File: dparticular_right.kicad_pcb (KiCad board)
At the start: 2 copper layers, 185.7 x 157.2 mm, 51 parts, among them J1 To Left Hand, SW1:10 Key_Ins, SW1:11 Key_Prnt, SW2:10 Key_F7, SW2:11 Key_F8, SW2:12 Key_F9, SW2:13 Key_F10, SW2:14 Key_F11, SW2:15 Key_F12, SW2:16 Key_Del, SW3:10 Key_7, SW3:11 Key_8, SW3:12 Key_9, SW3:13 Key_0, SW3:14 Key_Hyph, SW3:15 Key_Eql, SW3:16 Key_Bksp, SW3:9 Key_6, SW4:10 Key_U, SW4:11 Key_I, SW4:12 Key_O, SW4:13 Key_P, SW4:14 Key_LBrk, SW4:15 Key_RBrk, SW4:16 Key_BkSl, SW4:9 Key_Y, SW5:10 Key_J, SW5:11 Key_K, SW5:12 Key_L, SW5:13 Key_Semi, SW5:14 Key_Quot, SW5:16 Key_Entr, SW5:9 Key_H, SW6:10 Key_M, SW6:11 Key_Coma, SW6:12 Key_Per, SW6:13 Key_Slsh, SW6:14 Key_RShft, SW6:9 Key_N, SW7:11 Key_RAlt, SW7:12 Key_RWin, SW7:13 Key_Menu, SW7:14 Key_RCtrl, SW7:9 Key_RSpc, U1 MCP23018

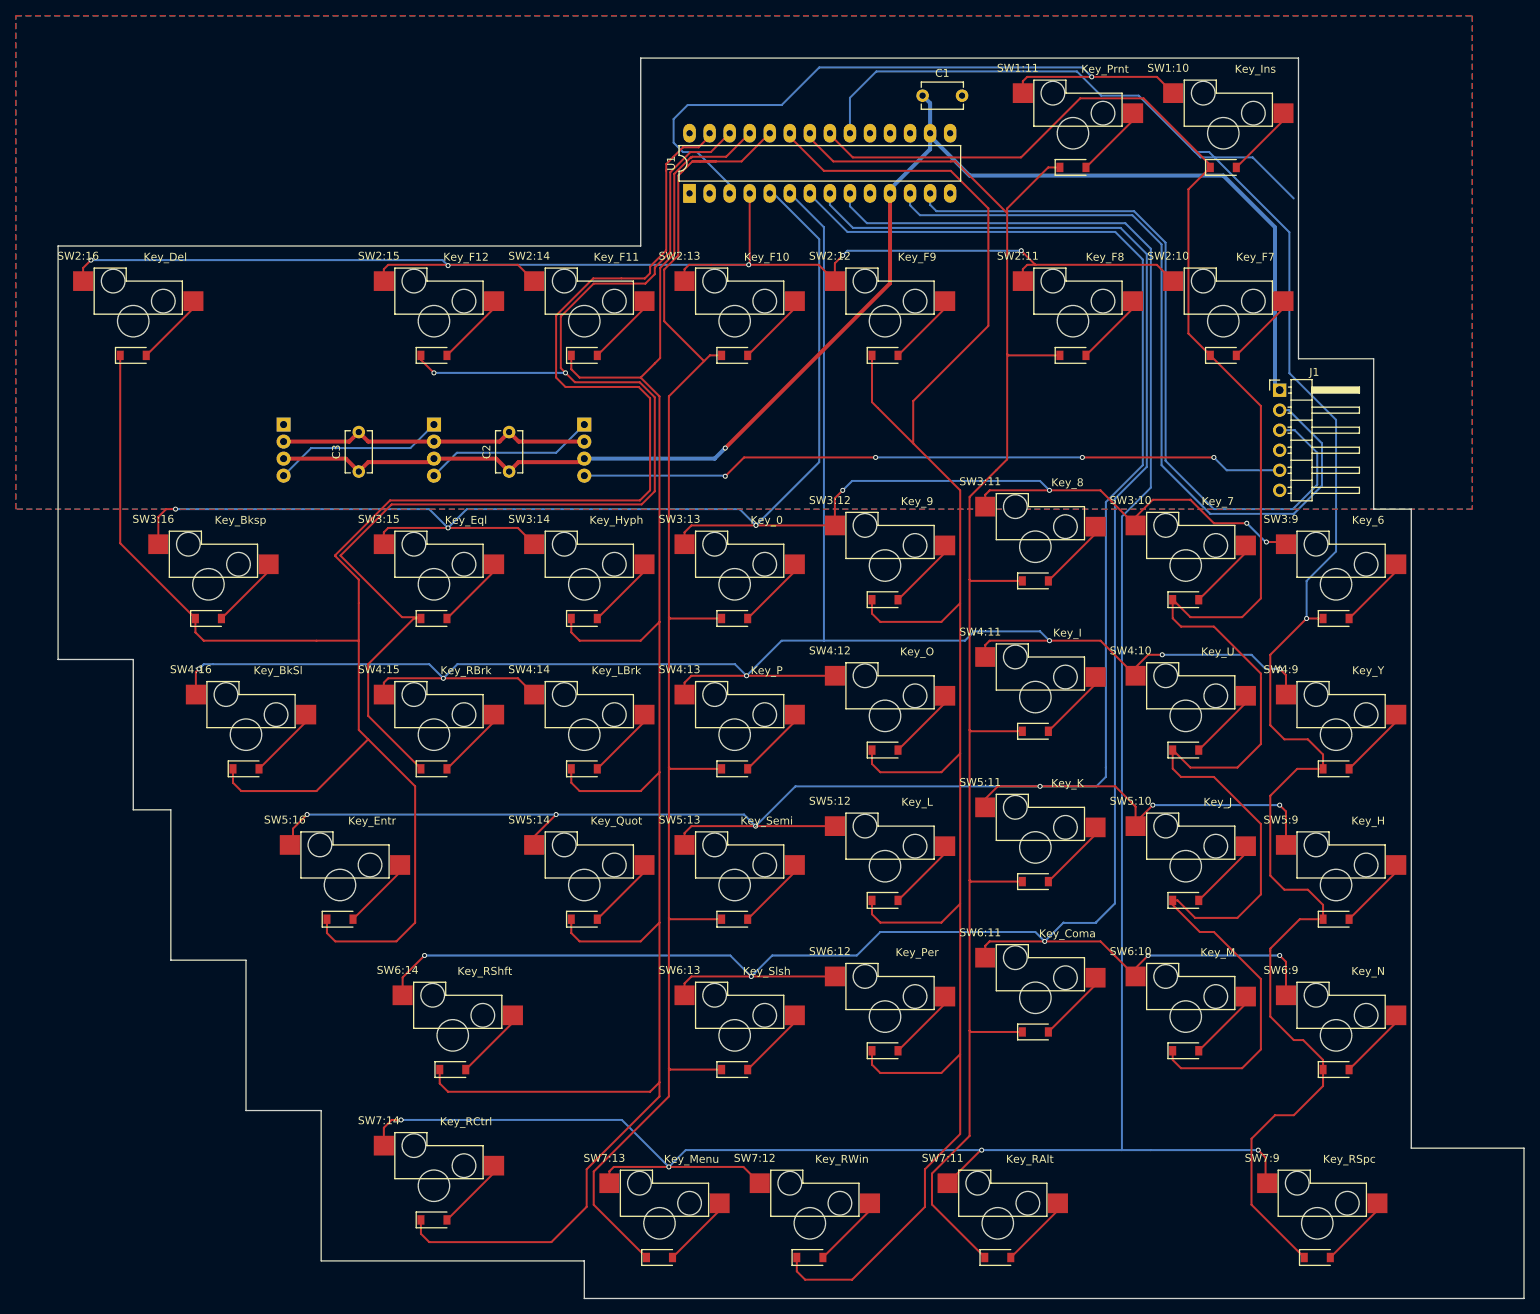
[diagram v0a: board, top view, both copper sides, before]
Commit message: Right hand: eliminate right angles in remaining columns
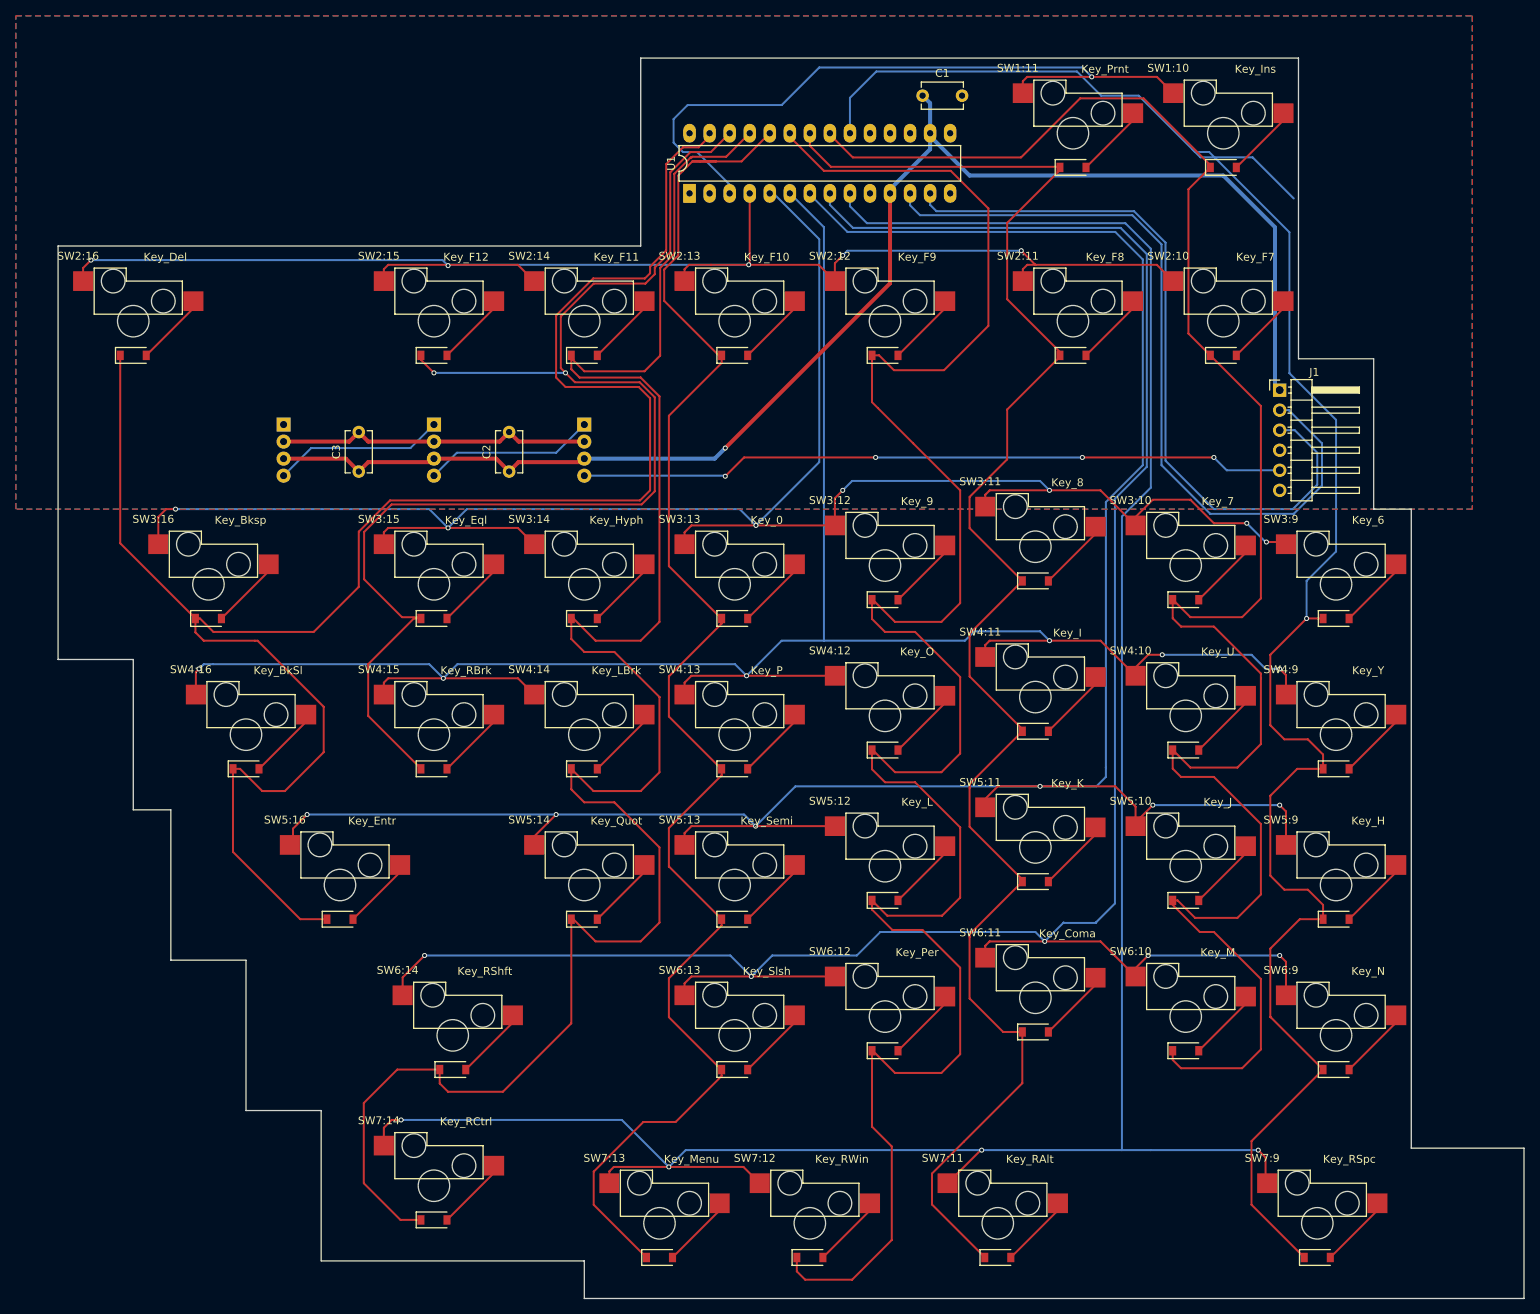
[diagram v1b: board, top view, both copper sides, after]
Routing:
- net /COL16: track 259.3 -> 244.1 mm
- net /COL12: track 257.1 -> 270.6 mm
- net /COL14: track 258.8 -> 250.5 mm
- net /COL13: track 194.8 -> 192.0 mm
- net /COL15: track 170.7 -> 168.2 mm
- net /COL9: track 253.7 -> 251.7 mm
- net /COL11: track 211.8 -> 211.1 mm

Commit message: Right hand: Eliminate all remaining right angles
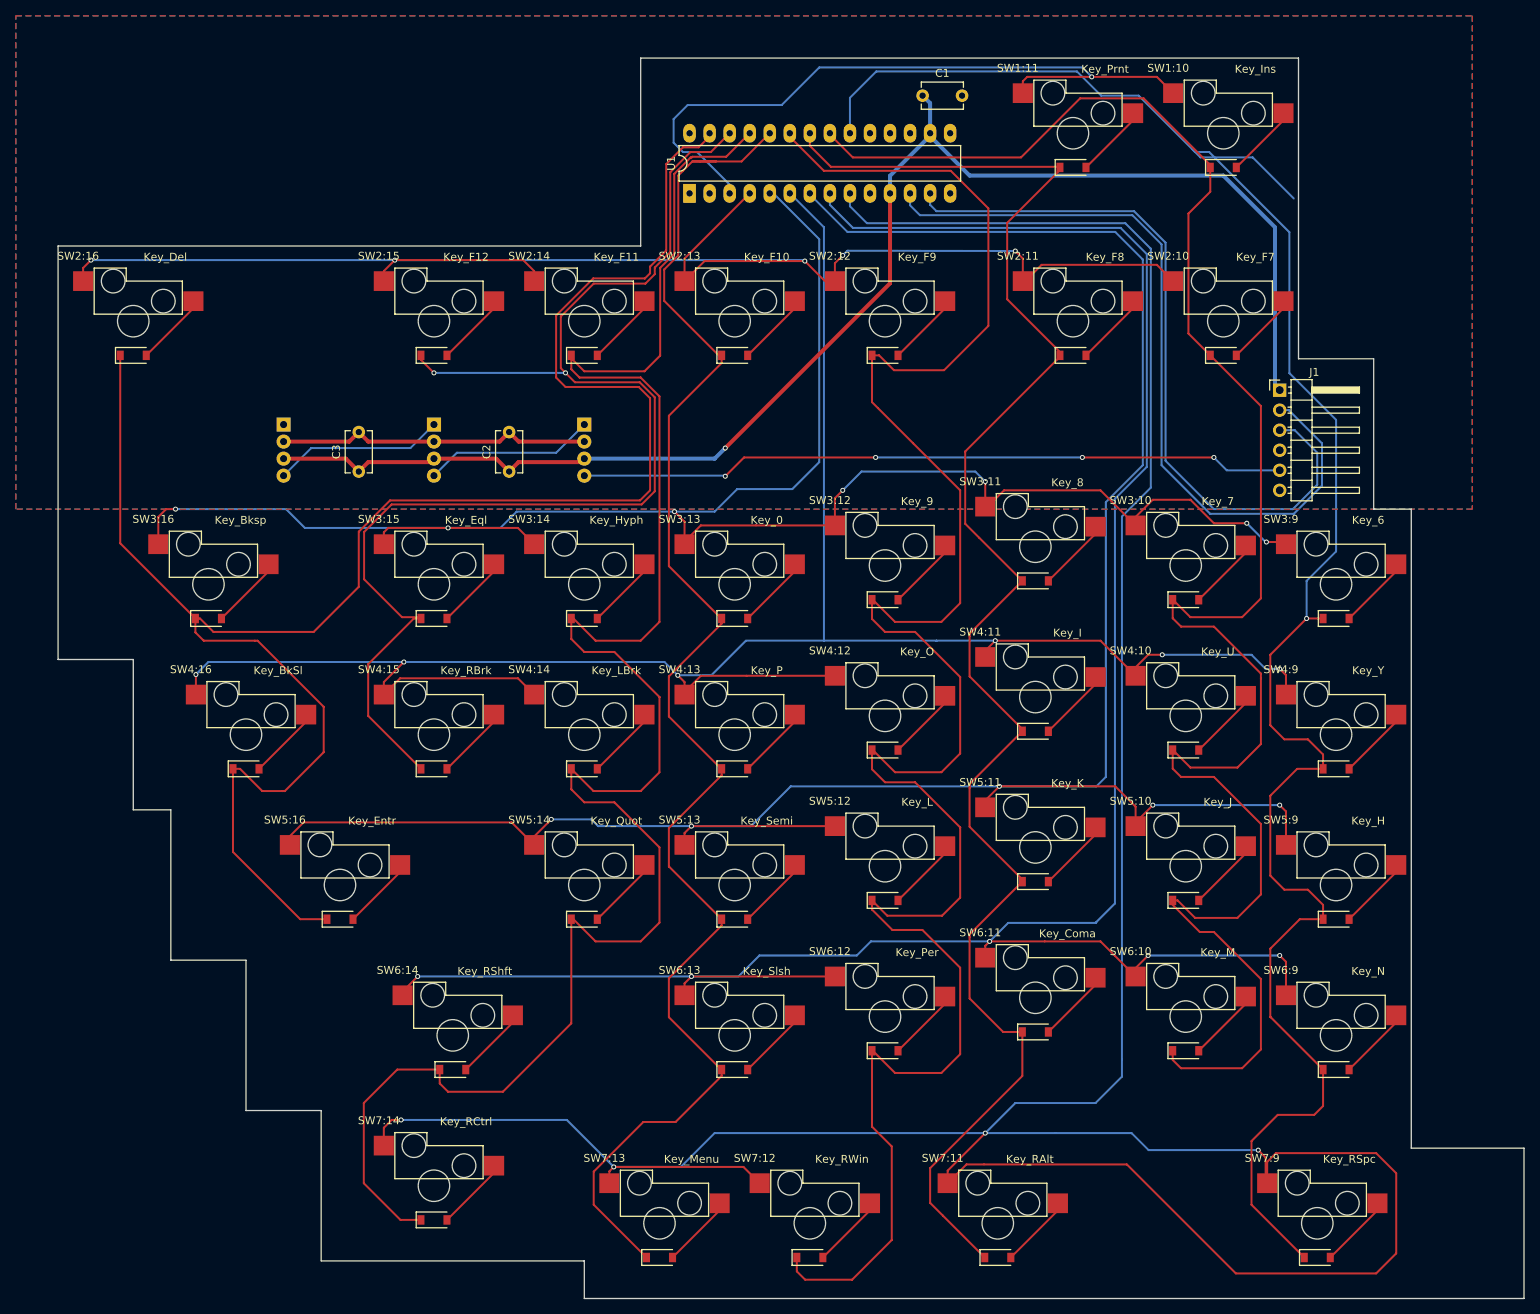
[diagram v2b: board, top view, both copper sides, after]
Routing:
- net /ROW7: track 306.9 -> 417.2 mm
- net /ROW2: track 189.8 -> 203.1 mm
- net /ROW6: track 297.0 -> 292.8 mm
- net /ROW4: track 264.3 -> 261.0 mm
- net /ROW3: track 251.3 -> 248.2 mm
- net /ROW5: track 297.6 -> 294.7 mm, vias 6 -> 5
- net /COL9: track 251.7 -> 254.4 mm
- net /COL11: track 211.1 -> 211.8 mm
